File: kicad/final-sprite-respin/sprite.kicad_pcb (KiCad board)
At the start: 4 copper layers, 35 x 35 mm, 70 parts, among them J1 M20-7910442R, U1 CC430F513X, U2 LSM9DS1, U3 SPRITETCXO_TCXO_7Z, U4 DRV8837, U5 ADP5092, U6 DRV8837, U7 DRV8837, U8 TASC, U9 TASC, X1 SPRITEPIN_SPRITE_PIN, X2 SPRITEPIN_SPRITE_PIN

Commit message: Prepare layout for spiral inductor
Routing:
- net /VBAT: track 68.7 -> 74.9 mm
- net Net-(L4-Pad2): track 56.6 -> 59.4 mm
- net /PWM1: track 66.3 -> 68.7 mm
- net /PWM2: track 62.9 -> 65.3 mm
- net Net-(L3-Pad1): track 39.0 -> 40.9 mm

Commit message: Route spiral inductor
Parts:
- turned R22 to 90 degrees
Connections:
- net Net-(R22-Pad1) renamed /SPIRAL
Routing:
- net /SPIRAL: track 3.38 -> 401.2 mm, vias 1 -> 3
- net GND: track 92.5 -> 93.5 mm, vias 18 -> 17
- net Net-(R22-Pad2): track 3.63 -> 2.71 mm
- net VCCINT: track 244.4 -> 243.8 mm

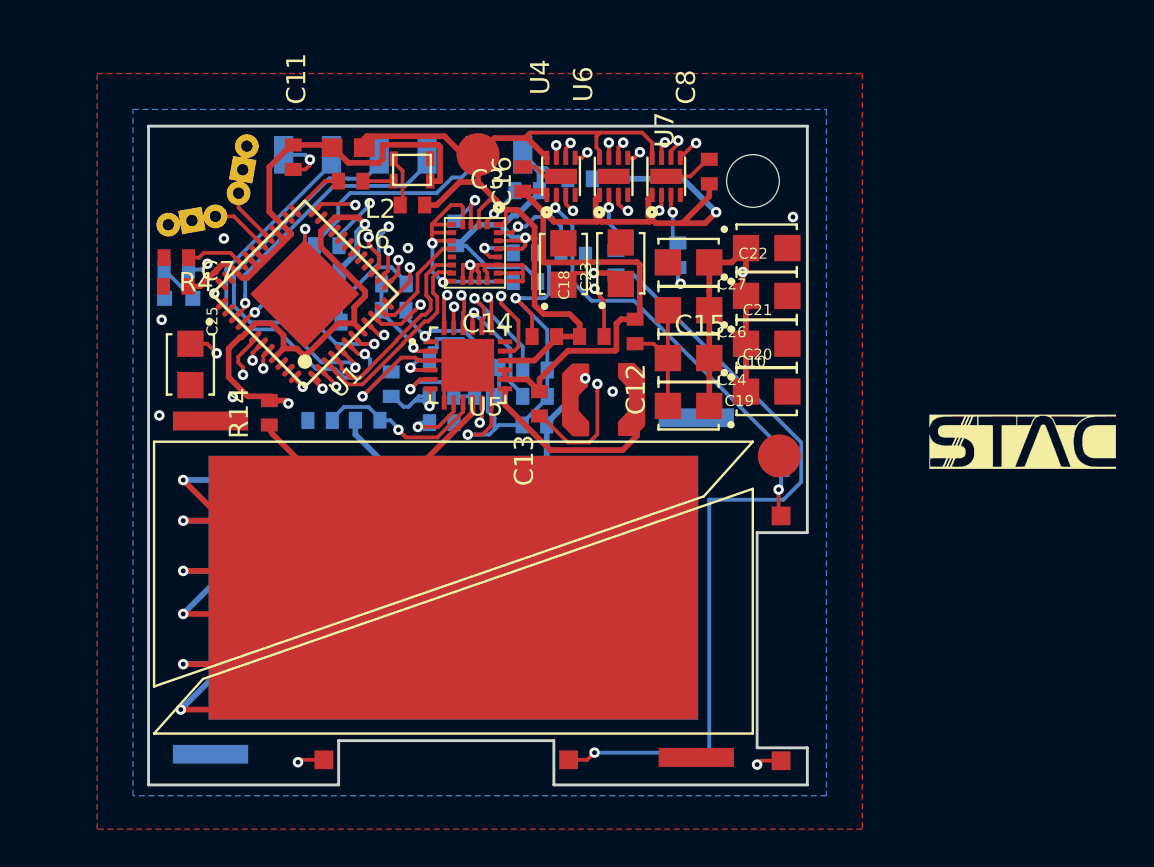
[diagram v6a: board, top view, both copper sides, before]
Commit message: updated pcb with spots for 6 more caps
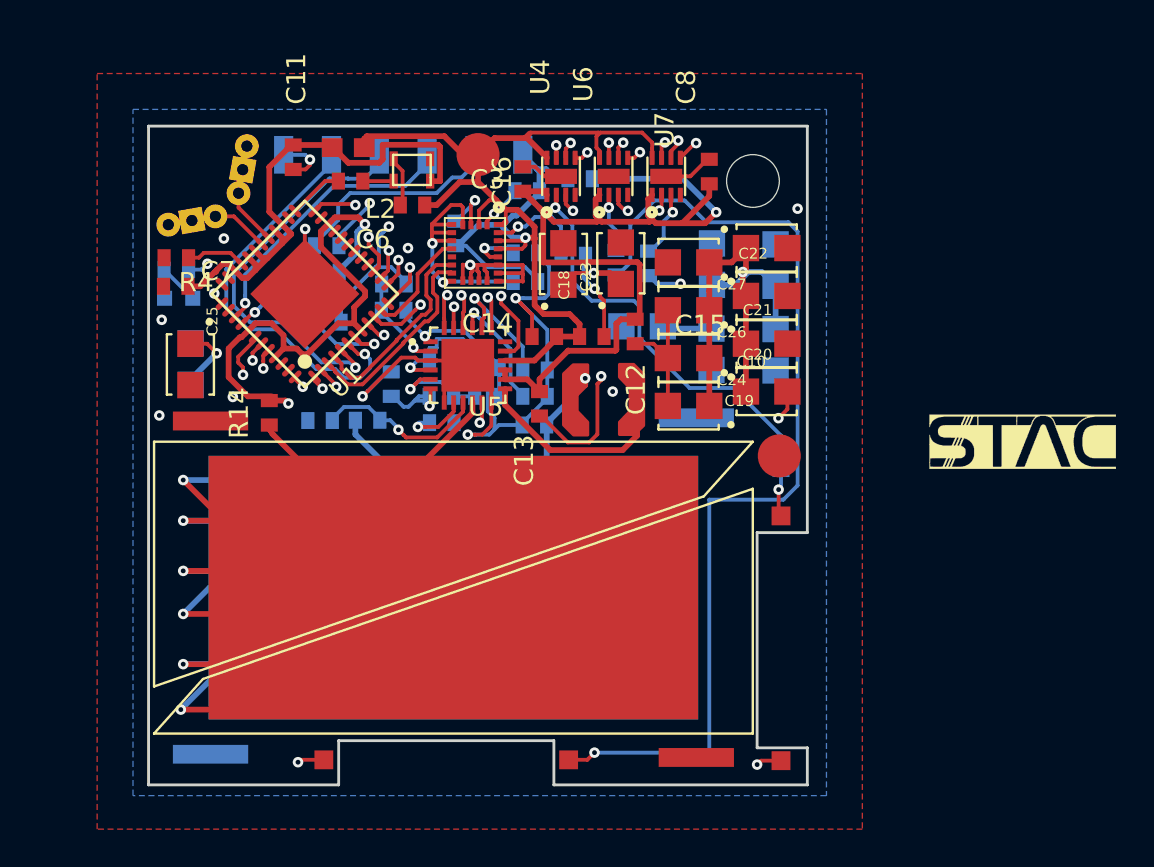
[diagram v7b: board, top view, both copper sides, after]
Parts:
- added C28: CPH3225A, sprite:CAPCP3225X100N, B.Cu at (154.1, 95.3)
- added C29: CPH3225A, sprite:CAPCP3225X100N, B.Cu at (150.8, 90.8)
- added C30: CPH3225A, sprite:CAPCP3225X100N, B.Cu at (154.1, 90.8)
- added C31: CPH3225A, sprite:CAPCP3225X100N, B.Cu at (123.1, 96.1)
- added C32: CPH3225A, sprite:CAPCP3225X100N, B.Cu at (150.7, 95.3)
- added C33: CPH3225A, sprite:CAPCP3225X100N, B.Cu at (147.1, 94.1)
- moved R22 1.62 mm to (147.4, 90.7)
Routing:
- net /VBAT: track 74.9 -> 88.7 mm
- net Net-(L4-Pad1): track 41.9 -> 52.8 mm
- net /SPIRAL: track 401.2 -> 409.8 mm
- net GND: track 93.5 -> 96.1 mm, vias 17 -> 18
- net Net-(R11-Pad1): track 19.7 -> 21.1 mm
- net Net-(R22-Pad2): track 2.71 -> 3.62 mm

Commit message: Clean up silkscreen
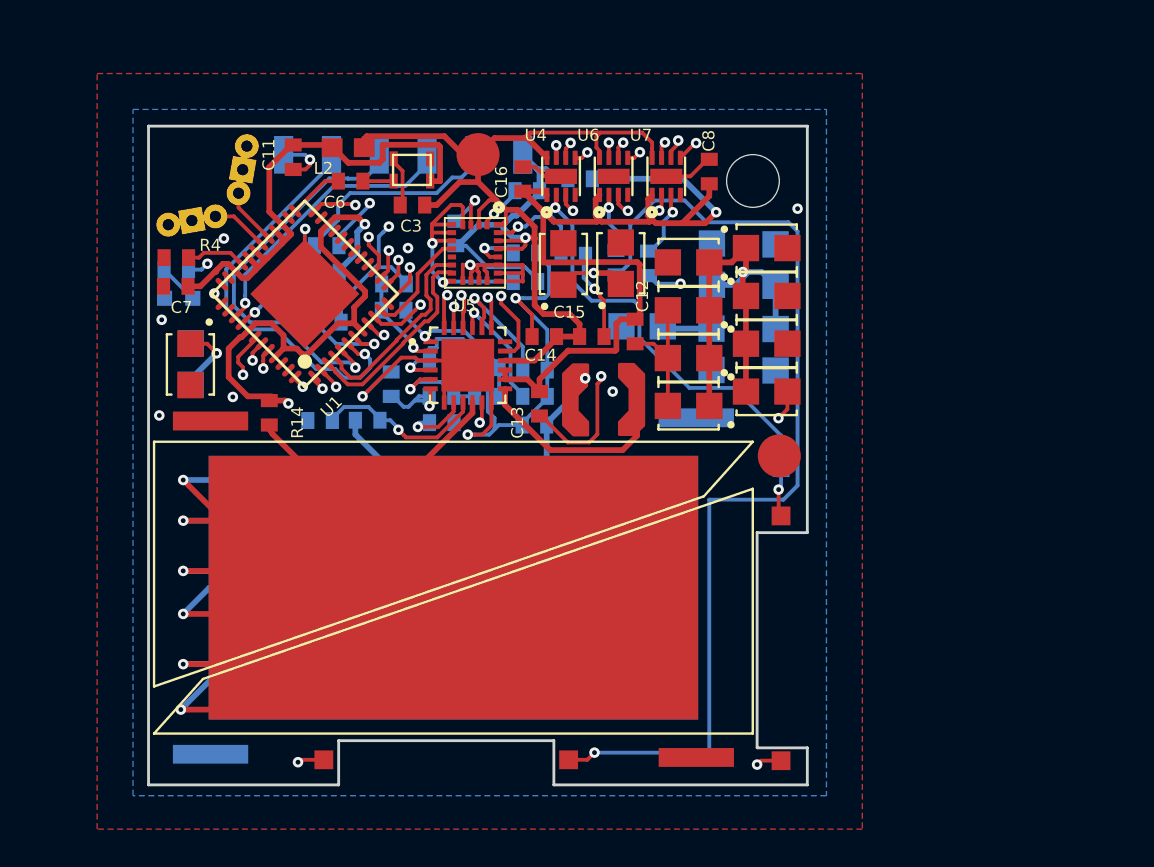
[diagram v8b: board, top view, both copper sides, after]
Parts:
- removed G***: LOGO, sprite:logo
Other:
- board text removed: "STAC Spinor in Space!"
